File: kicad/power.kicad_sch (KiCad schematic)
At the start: 92 parts, among them J1 12 V in, J2 TX power (shunt), U1 TPS54202DDCR, U2 TPS65131RGER, U3 TPS7A4701RGWR, U4 TPS7A3301RGWR, U5 LM2731XMF, U6 TLV1117-33

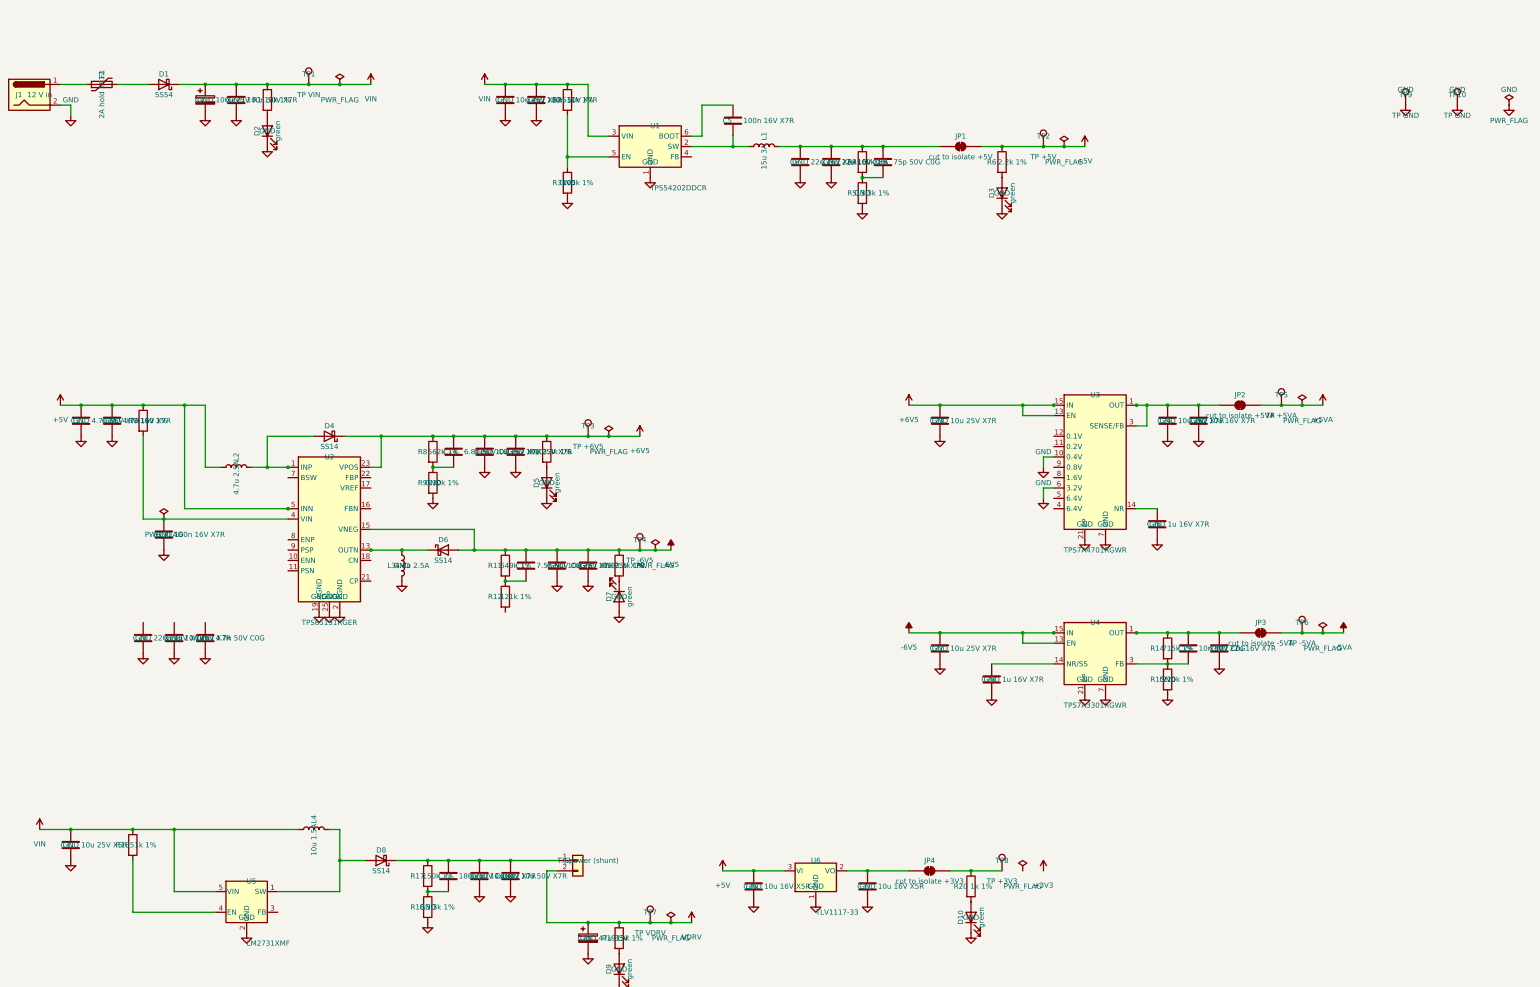
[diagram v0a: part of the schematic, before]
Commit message: AD7606C-16, one sheet per repeated block, clock buffering, first simulations
- ADC: AD7606C-16 in software mode (OS pins high, WR held high, DB11/SDI on
  shared ADC_SDI), 33 R source resistors on DOUTA/DOUTB/BUSY.
- Every repeated block is its own reused sheet: tx_group x16, en_buf x4,
  clk_buf x7, mic x8 (replaces tx_shift, tx_drivers, mems). Sheets other than
  channel are generated by scripts/build_cells.py and scripts/build_power.py.
- Headers: GND conductors either side of every clock, ADC_SDI, idle pulls,
  DNP RC terminations as fallback.
- Power: 3V3_MIC ferrite filter moved to the power sheet with LED, test point
  and flag.
- Simulations (LTspice, sim/): RX chain gain/noise, TX burst and recovery,
  clock signal integrity; results in docs/simulation-1.md. FPGA ribbon outputs
  changed to DRIVE 4 after simulation.
- Brief, CLAUDE.md, review status and SKiDL reference spec updated.
  ERC: 0 violations, 1,701 parts.
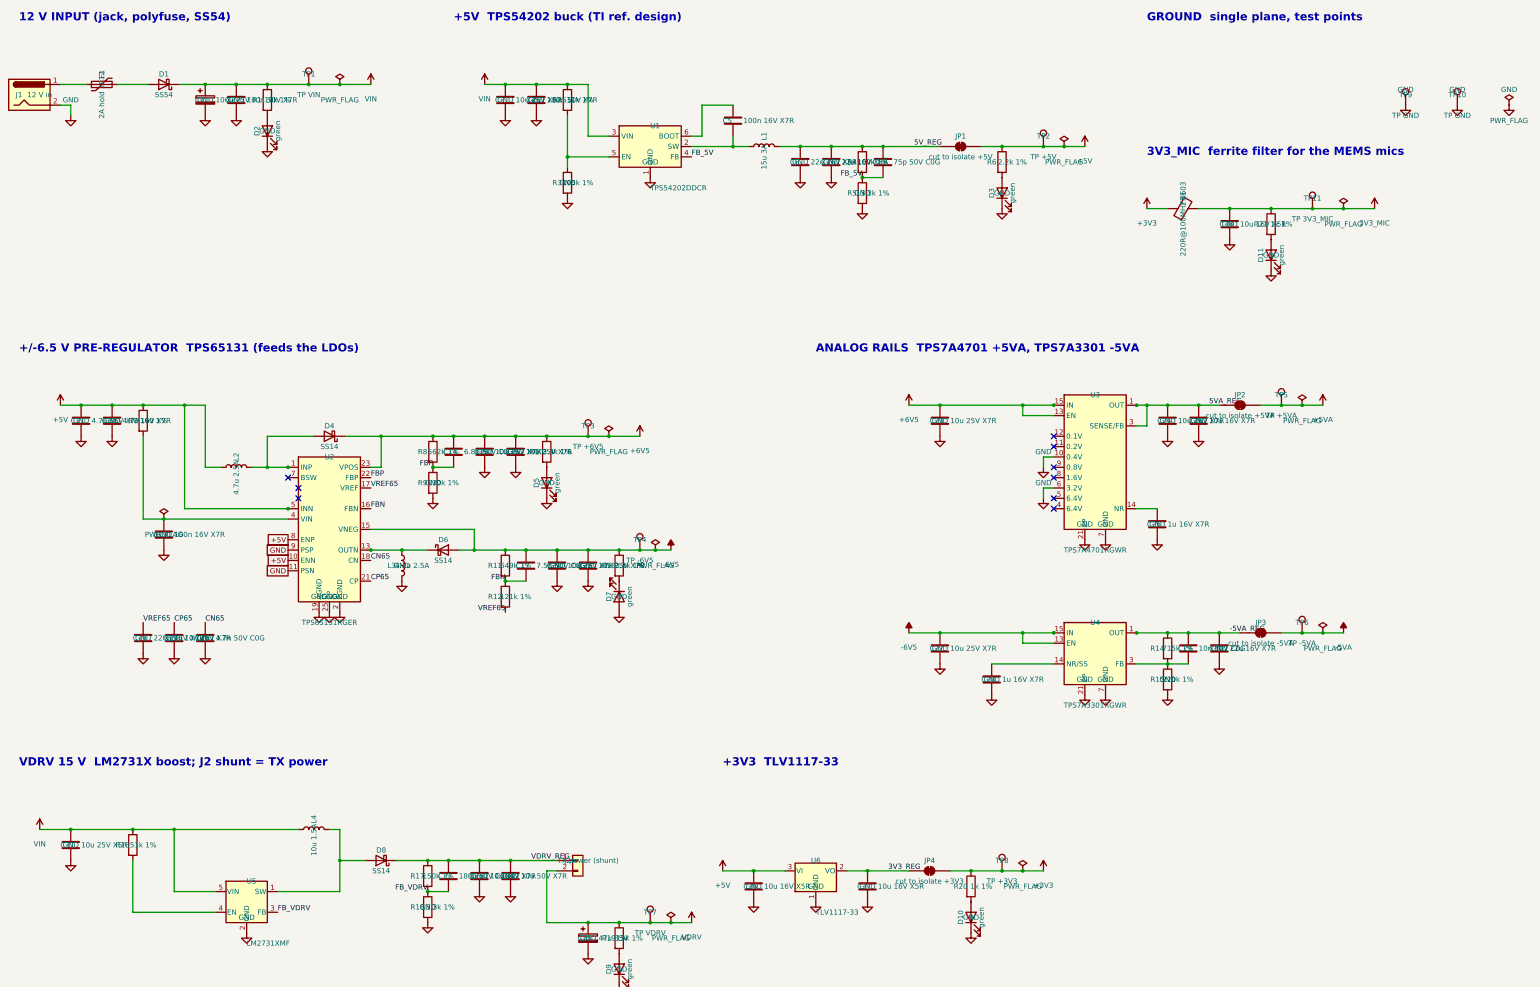
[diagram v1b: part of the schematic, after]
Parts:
- added C38: 10u 16V X5R, Capacitor_SMD:C_0805_2012Metric, symbol Device:C
- added D11: green, LED_SMD:LED_0603_1608Metric, symbol Device:LED
- added FB1: 220R@100MHz 0603, Inductor_SMD:L_0603_1608Metric, symbol Device:FerriteBead
- added R21: 1k 1%, Resistor_SMD:R_0603_1608Metric, symbol Device:R
- added TP11: TP 3V3_MIC, TestPoint:TestPoint_Pad_D1.5mm, symbol Connector:TestPoint
- C1, C11, C12, C13, C14, C15, C16, C17, C18, C19, C2, C20, C21, C22, C23, C24, C25, C26, C27, C28, C29, C3, C30, C31, C32, C33, C34, C35, C36, C37, C4, C5, C6, C7, C8, D1, D10, D2, D3, D4, D5, D6, D7, D8, D9, F1, J1, J2, JP1, JP2, JP3, JP4, L1, L2, L3, L4, R1, R10, R11, R12, R13, R14, R15, R16, R17, R18, R19, R2, R20, R3, R4, R5, R6, R7, R8, R9, TP1, TP10, TP2, TP3, TP4, TP5, TP6, TP7, TP8, TP9, U1, U2, U3, U4, U5, U6: LCSC (none) -> TBD
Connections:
- net +3V3: now also JP4.2 (B), R20.1, TP8.1, FB1.1
- net +5V: now also U2.10 (ENN), U2.8 (ENP)
- net GND: now also U2.11 (PSN), U2.9 (PSP), C38.2, D11.1 (K)
- net -5VA_REG: now reaches C29.1, C30.1, JP3.1 (A), R14.1, U4.1 (OUT), U4.20 (OUT)
- net 5VA_REG: now reaches C24.1, C25.1, JP2.1 (A), U3.1 (OUT), U3.20 (OUT), U3.3 (SENSE/FB)
- net FBN: now reaches C17.2, R11.2, R12.1
- net FBN: now also U2.16 (FBN)
- net VREF65: now reaches R12.2
- net VREF65: now also C18.1, U2.17 (VREF)
- net FB_VDRV: now reaches U5.3 (FB)
- net FB_VDRV: now also C32.2, R17.2, R18.1
- net 5V_REG: now reaches C6.1, C7.1, C8.1, JP1.1 (A), L1.2, R4.1
- net CN65: now reaches U2.18 (CN)
- net CN65: now also C20.1
- net CP65: now reaches U2.21 (CP)
- net CP65: now also C19.1
- net FBP: now reaches U2.22 (FBP)
- net FBP: now also C14.2, R8.2, R9.1
- net FB_5V: now reaches C8.2, R4.2, R5.1
- net FB_5V: now also U1.4 (FB)
- net 3V3_REG: now reaches C37.1, JP4.1 (A), U6.2 (VO)
- net VDRV_REG: now reaches C32.1, C33.1, C34.1, D8.1 (K), J2.1 (Pin_1), R17.1
- new net: D11.2 (A), R21.2
- new net 3V3_MIC: C38.1, FB1.2, R21.1, TP11.1
- no-connect marks 0 -> 9
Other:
- note added: "+/-6.5 V PRE-REGULATOR TPS65131 (feeds the LDOs)"
- note added: "+3V3 TLV1117-33"
- note added: "+5V TPS54202 buck (TI ref. design)"
- note added: "12 V INPUT (jack, polyfuse, SS54)"
- note added: "3V3_MIC ferrite filter for the MEMS mics"
- note added: "ANALOG RAILS TPS7A4701 +5VA, TPS7A3301 -5VA"
- note added: "GROUND single plane, test points"
- note added: "VDRV 15 V LM2731X boost; J2 shunt = TX power"

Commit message: Block-diagram top page, power review fixes, readable sheets
Top level
- Page 1 is now a block diagram of the signal flow (FPGA -> headers ->
  clock buffers / TX drive -> transceivers -> ADCs -> FPGA, mics, power).
- New group sheets hold the reused cells: tx (16 tx_group + 4 en_buf),
  array (64 channel), adcs (8 adc), mics (8 mic), clocks (7 clk_buf).
  Power and headers stay directly under the top. All written by gen_top.py,
  which now also survives a kicad-cli re-save of a cell sheet.

Power (review findings)
- Polyfuse 1812L200/16DR (16 V), TPS65131RGER stated explicitly, input caps
  2 x 10u 1206, 50 V caps on 12 V, inductor values carry minimum Isat.
- +3V3: TLV75733P (ceramic-stable) replaces TLV1117-33.
- New JP5/JP6 isolate +-6V5; every rail: REG node -> jumper -> rail with TP,
  LED (not on analog LDOs) and PWR_FLAG.
- Power sheet is now generated by build_cells.py in a 2x3 block layout
  (build_power.py removed).

Readability and small fixes
- Rails on sideways pins use labelled flags; sideways GND symbols hide text.
- tx_group: 595 outputs wired straight to the drivers.
- Title blocks on every sheet; channel sheet notes and field placement fixed
  (sch_fields.py --only, sch_annotate.py).
- ADC_SDI 10k pull-down, ADC reset/DOUT notes, mic cap 50 V.
- ERC 0 violations, 1,704 parts. PDFs: docs/schematics/00..13.
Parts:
- removed U6: TLV1117-33, Package_TO_SOT_SMD:SOT-223-3_TabPin2, symbol Regulator_Linear:TLV1117-33
- added JP5: cut to isolate +6V5, Jumper:SolderJumper-2_P1.3mm_Bridged_RoundedPad1.0x1.5mm, symbol Jumper:SolderJumper_2_Bridged
- added JP6: cut to isolate -6V5, Jumper:SolderJumper-2_P1.3mm_Bridged_RoundedPad1.0x1.5mm, symbol Jumper:SolderJumper_2_Bridged
- added U6: TLV75733PDBVR, Package_TO_SOT_SMD:SOT-23-5, symbol Regulator_Linear:TLV75733PDBV
- C11, C12: value 4.7u 16V X7R -> 10u 16V X7R 1206; footprint Capacitor_SMD:C_0805_2012Metric -> Capacitor_SMD:C_1206_3216Metric
- C15, C16, C21, C22, C23, C27: value 10u 25V X7R -> 10u 25V X7R 1206
- C24, C25: value 10u 16V X7R -> 10u 16V X7R 1206
- C3, C31: value 10u 25V X5R -> 10u 50V X7R 1210; footprint Capacitor_SMD:C_1206_3216Metric -> Capacitor_SMD:C_1210_3225Metric
- C30: value 22u 16V X7R -> 22u 16V X7R 1210
- C33, C34: value 10u 50V X7R -> 10u 50V X7R 1210
- C37: value 10u 16V X5R -> 10u 16V X7R
- C6, C7: value 22u 16V X5R -> 22u 16V X5R 1206
- F1: value 2A hold 1812 -> 1812L200/16DR 2A 16V
- J1: value 12 V in -> 12 V in (5.5x2.1)
- L1: value 15u 3A -> 15u Isat>=3.5A; footprint Inductor_SMD:L_Bourns_SRN6045TA -> Inductor_SMD:L_Bourns_SRN8040TA
- L2, L3: value 4.7u 2.5A -> 4.7u Isat>=2A
- L4: value 10u 1.5A -> 10u Isat>=2A
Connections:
- net +5V: now also U6.1 (IN), U6.3 (EN)
- net +6V5: now also JP5.2 (B); no longer C14.1, C15.1, C16.1, D4.1 (K), R8.1, U2.23 (VPOS)
- net -6V5: now also JP6.2 (B); no longer C17.1, C21.1, C22.1, D6.2 (A), R11.1, U2.15 (VNEG)
- net 3V3_REG: now also U6.5 (OUT)
- net GND: now also U6.2 (GND)
- net SW_N: now reaches D6.1 (K), L3.1, U2.13 (OUTN), U2.14 (OUTN)
- net VIN65: now reaches C13.1, R7.2, U2.4 (VIN)
- net VIN_JACK: now reaches F1.1, J1.1
- net LED_VIN: now reaches D2.2 (A), R1.2
- net LED_+5V: now reaches D3.2 (A), R6.2
- net NR_5VA: now reaches C26.1, U3.14 (NR)
- net FB_M5VA: now reaches C29.2, R14.2, R15.1, U4.3 (FB)
- net LED_+3V3: now reaches D10.2 (A), R20.2
- net VIN_FUSED: now reaches D1.2 (A), F1.2
- net LED_3V3_MIC: now reaches D11.2 (A), R21.2
- net NR_M5VA: now reaches C28.1, U4.14 (NR/SS)
- net LED_+6V5: now reaches D5.2 (A), R10.2
- net SW_P: now reaches D4.2 (A), L2.2, U2.1 (INP), U2.24 (INP)
- net LED_VDRV: now reaches D9.2 (A), R19.2
- net LED_-6V5: now reaches D7.1 (K), R13.2
- net SW_VDRV: now reaches D8.2 (A), L4.2, U5.1 (SW)
- net SW_5V: now reaches C5.2, L1.1, U1.2 (SW)
- net EN_5V: now reaches R2.2, R3.1, U1.5 (EN)
- net BOOT_5V: now reaches C5.1, U1.6 (BOOT)
- net EN_VDRV: now reaches R16.2, U5.4 (EN)
- new net -6V5_REG: C17.1, C21.1, C22.1, D6.2 (A), JP6.1 (A), R11.1, U2.15 (VNEG)
- new net 6V5_REG: C14.1, C15.1, C16.1, D4.1 (K), JP5.1 (A), R8.1, U2.23 (VPOS)
- no-connect marks 9 -> 10
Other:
- note added: "+5VA: ANY-OUT 1.4 + 3.2 + 0.4 = 5.0 V. -5VA = -1.176 V x (1 + 715k/220k) = -5.00 V."
- note added: "+6V5 = 1.213 V x (1 + 562k/130k) = 6.46 V. -6V5 = -1.213 V x 649k/121k = -6.51 V."
- note added: "1.23 V x (1 + 150k/13.3k) = 15.1 V. Load: 64 elements CW at 40 kHz, CV^2f = 1.3 W, about 0.12 A."
- note added: "A. 12 V INPUT: jack, polyfuse (16 V), SS54 reverse-polarity diode -> VIN"
- note added: "B. +5V: TPS54202 buck (TI reference design), 2 A"
- note added: "C. +-6V5: TPS65131RGER boost + inverter from +5V (feeds the analog LDOs only)"
- note added: "D. ANALOG RAILS: TPS7A4701 +5VA, TPS7A3301 -5VA (low noise, no LEDs)"
- note added: "Drawn with the pin-identical TPS65130 symbol: order TPS65131RGER (2 A switches). PSP/PSN low: fixed-frequency PWM."
- note added: "E. VDRV 15 V: LM2731X boost from VIN. Remove the J2 shunt to unpower all TX drivers"
- note added: "F. +3V3: TLV75733P LDO from +5V (1 A, stable with ceramic caps)"
- note added: "G. GROUND: one GND net and plane"
- note added: "H. 3V3_MIC: ferrite-filtered supply for the 8 MEMS mics (remove FB1 to isolate)"
- note added: "Load < 0.15 A: ADC VDRIVE, clock buffers, logic, mics."
- note added: "Load: 64 x OPA1678 (4 mA per channel) + 8 x AD7606C AVCC: about 0.45 A on +5VA, 0.3 A on -5VA."
- note added: "Test points for scope grounds."
- note added: "Use a regulated 12 V adapter only: LM2731 VIN max 14 V. Jack 5.5 x 2.1 mm, >= 1.5 A."
- note added: "Vout = 0.596 V x (1 + 100k/13.3k) = 5.08 V. EN UVLO about 7 V. Load about 1.4 A."
- note removed: "+/-6.5 V PRE-REGULATOR TPS65131 (feeds the LDOs)"
- note removed: "+3V3 TLV1117-33"
- note removed: "+5V TPS54202 buck (TI ref. design)"
- note removed: "12 V INPUT (jack, polyfuse, SS54)"
- note removed: "3V3_MIC ferrite filter for the MEMS mics"
- note removed: "ANALOG RAILS TPS7A4701 +5VA, TPS7A3301 -5VA"
- note removed: "GROUND single plane, test points"
- note removed: "VDRV 15 V LM2731X boost; J2 shunt = TX power"
- company: (none) -> Hybrid 8x8 ultrasonic AESA
- title: (none) -> Power: 12 V in, +5V, +-6V5, +-5VA, VDRV, +3V3, 3V3_MIC

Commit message: more updates on schematics
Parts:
- F1: value 1812L200/16DR 2A 16V -> 1812L200/16DR
- JP1: value cut to isolate +5V -> cut to isolate
- JP2: value cut to isolate +5VA -> cut to isolate
- JP3: value cut to isolate -5VA -> cut to isolate
- JP4: value cut to isolate +3V3 -> cut to isolate
- JP5: value cut to isolate +6V5 -> cut to isolate
- JP6: value cut to isolate -6V5 -> cut to isolate
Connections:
- net -5VA_REG: no longer names the net of C29.1, C30.1, JP3.1 (A), R14.1, U4.1 (OUT), U4.20 (OUT)
- net -6V5_REG: no longer names the net of C21.1, C22.1, D6.2 (A), JP6.1 (A), U2.15 (VNEG)
- net -6V5_REG: now also C17.2, R11.2; no longer C17.1, R11.1
- net 3V3_REG: no longer names the net of C37.1, JP4.1 (A), U6.5 (OUT)
- net 5VA_REG: no longer names the net of C24.1, C25.1, JP2.1 (A), U3.1 (OUT), U3.20 (OUT), U3.3 (SENSE/FB)
- net 5V_REG: no longer names the net of C6.1, C7.1, C8.1, JP1.1 (A), L1.2, R4.1
- net 6V5_REG: no longer names the net of C14.1, C15.1, C16.1, D4.1 (K), JP5.1 (A), R8.1, U2.23 (VPOS)
- net BOOT_5V: no longer names the net of C5.1, U1.6 (BOOT)
- net CN65: no longer names the net of C20.1, U2.18 (CN)
- net CP65: no longer names the net of C19.1, U2.21 (CP)
- net EN_5V: no longer names the net of R2.2, R3.1, U1.5 (EN)
- net EN_VDRV: no longer names the net of R16.2, U5.4 (EN)
- removed net FBN: C17.2, R11.2, R12.1, U2.16 (FBN)
- net FBP: no longer names the net of C14.2, R8.2, R9.1, U2.22 (FBP)
- net FB_5V: no longer names the net of C8.2, R4.2, R5.1, U1.4 (FB)
- net FB_M5VA: no longer names the net of C29.2, R14.2, R15.1, U4.3 (FB)
- net FB_VDRV: no longer names the net of C32.2, R17.2, R18.1, U5.3 (FB)
- net LED_+3V3: no longer names the net of D10.2 (A), R20.2
- net LED_+5V: no longer names the net of D3.2 (A), R6.2
- net LED_+6V5: no longer names the net of D5.2 (A), R10.2
- net LED_-6V5: no longer names the net of D7.1 (K), R13.2
- net LED_3V3_MIC: no longer names the net of D11.2 (A), R21.2
- net LED_VDRV: no longer names the net of D9.2 (A), R19.2
- net LED_VIN: no longer names the net of D2.2 (A), R1.2
- net NR_5VA: no longer names the net of C26.1, U3.14 (NR)
- net NR_M5VA: no longer names the net of C28.1, U4.14 (NR/SS)
- net SW_5V: no longer names the net of C5.2, L1.1, U1.2 (SW)
- net SW_N: no longer names the net of D6.1 (K), L3.1, U2.13 (OUTN), U2.14 (OUTN)
- net SW_P: no longer names the net of D4.2 (A), L2.2, U2.1 (INP), U2.24 (INP)
- net SW_VDRV: no longer names the net of D8.2 (A), L4.2, U5.1 (SW)
- net VDRV_REG: no longer names the net of C32.1, C33.1, C34.1, D8.1 (K), J2.1 (Pin_1), R17.1
- net VIN65: no longer names the net of C13.1, R7.2, U2.4 (VIN)
- net VIN_FUSED: no longer names the net of D1.2 (A), F1.2
- net VIN_JACK: no longer names the net of F1.1, J1.1
- net VREF65: no longer names the net of C18.1, U2.17 (VREF)
- net VREF65: now also R12.1; no longer R12.2
- new net: C17.1, R11.1, R12.2, U2.16 (FBN)
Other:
- note added: "Use a regulated 12 V adapter only (LM2731 VIN max 14 V). Jack 5.5 x 2.1 mm, >= 1.5 A."
- note removed: "Use a regulated 12 V adapter only: LM2731 VIN max 14 V. Jack 5.5 x 2.1 mm, >= 1.5 A."

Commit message: Design checker, wired power sheet, schematic-driven simulations
Checks
- scripts/check_design.py audits the netlist and writes docs/design-check.md:
  ERC, part counts, footprints vs pins, LCSC status, TX chain of all 64
  elements, RX chain and ADC wiring, clock fan-out, header pin map, 3.3 V
  levels on FPGA pins, supply rails, decoupling, capacitor ratings, polarity,
  regulator outputs from the divider values, rail testability, power budget.
  16 pass, 1 warning (LCSC numbers still TBD).
- scripts/pinmap.py: header pin maps shared by the builder and the checker.

Power sheet
- Redrawn conventionally: each regulator with its parts wired around it,
  key nodes named, power symbols only at the section edges; junction dots.
- VDRV load note corrected to about 0.24 A (simulated CW).

Simulations
- Channel circuit is exported from kicad/channel.kicad_sch (Sim.* fields set
  by scripts/sch_sim.py, models in sim/models/aesa_parts.lib) before every
  run; testbenches hold only stimulus, loads and measurements.
- New: rx_mc (200-channel Monte Carlo), rx_overload, tx_cw, mic_supply.
  All 10 testbenches pass (sim/reports/README.md).
- CW finding: 3.7 mA per element (RX limiter 19 mW), 0.24 A for all 64;
  budget updated in the checker and the brief.
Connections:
- net 5VA_REG: now reaches C24.1, C25.1, JP2.1 (A), U3.1 (OUT), U3.20 (OUT), U3.3 (SENSE/FB)
- net VDRV_REG: now reaches C32.1, C33.1, C34.1, D8.1 (K), J2.1 (Pin_1), R17.1
- net FB_VDRV: now reaches C32.2, R17.2, R18.1, U5.3 (FB)
- net SW_N: now reaches D6.1 (K), L3.1, U2.13 (OUTN), U2.14 (OUTN)
- net -6V5_REG: now reaches C17.2, C21.1, C22.1, D6.2 (A), JP6.1 (A), R11.2, U2.15 (VNEG)
- net FB_M5VA: now reaches C29.2, R14.2, R15.1, U4.3 (FB)
- net LED_+5V: now reaches D3.2 (A), R6.2
- net 5V_REG: now reaches C6.1, C7.1, C8.1, JP1.1 (A), L1.2, R4.1
- net FB_5V: now reaches C8.2, R4.2, R5.1, U1.4 (FB)
- net 6V5_REG: now reaches C14.1, C15.1, C16.1, D4.1 (K), JP5.1 (A), R8.1, U2.23 (VPOS)
- net FBP: now reaches C14.2, R8.2, R9.1, U2.22 (FBP)
- net FBN: now reaches C17.1, R11.1, R12.2, U2.16 (FBN)
- net NR_M5VA: now reaches C28.1, U4.14 (NR/SS)
- net SW_VDRV: now reaches D8.2 (A), L4.2, U5.1 (SW)
- net VIN_JACK: now reaches F1.1, J1.1
- net LED_3V3_MIC: now reaches D11.2 (A), R21.2
- net 3V3_REG: now reaches C37.1, JP4.1 (A), U6.5 (OUT)
- net CN65: now reaches C20.1, U2.18 (CN)
- net EN_5V: now reaches R2.2, R3.1, U1.5 (EN)
- net LED_+6V5: now reaches D5.2 (A), R10.2
- net LED_+3V3: now reaches D10.2 (A), R20.2
- net -5VA_REG: now reaches C29.1, C30.1, JP3.1 (A), R14.1, U4.1 (OUT), U4.20 (OUT)
- net LED_VDRV: now reaches D9.2 (A), R19.2
- net NR_5VA: now reaches C26.1, U3.14 (NR)
- net LED_-6V5: now reaches D7.1 (K), R13.2
- net VIN_FUSED: now reaches D1.2 (A), F1.2
- net EN_VDRV: now reaches R16.2, U5.4 (EN)
- net VIN65: now reaches C13.1, R7.2, U2.4 (VIN)
- net SW_5V: now reaches C5.2, L1.1, U1.2 (SW)
- net BOOT_5V: now reaches C5.1, U1.6 (BOOT)
- net LED_VIN: now reaches D2.2 (A), R1.2
- net SW_P: now reaches D4.2 (A), L2.2, U2.1 (INP), U2.24 (INP)
- net VREF65: now reaches C18.1, R12.1, U2.17 (VREF)
- net CP65: now reaches C19.1, U2.21 (CP)
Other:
- note added: "1.23 V x (1 + 150k/13.3k) = 15.1 V. Load, all 64 elements in CW at 40 kHz: about 0.24 A (sim/reports/tx_cw.md)."
- note removed: "1.23 V x (1 + 150k/13.3k) = 15.1 V. Load: 64 elements CW at 40 kHz, CV^2f = 1.3 W, about 0.12 A."
